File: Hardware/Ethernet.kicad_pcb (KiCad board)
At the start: 2 copper layers, 34 x 34 mm, 41 parts, among them J3 Conn_01x02_Male, J4 Conn_01x02_Male, J5 Conn_01x02_Male, J6 Conn_01x02_Male, J7 Conn_01x08_Male, J9 QWIIC_Stackable, U1 W5500, Y1 25MHz_SMD_Crystal_Resonator

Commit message: Working on SPI
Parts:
- moved R2 4.16 mm to (93.2, 93.0), turned to 180 degrees
- moved RN1 2.04 mm to (91.7, 86.0)
- moved RN2 2.01 mm to (91.7, 89.7)
- moved R6 1.08 mm to (93.0, 100.4)
- moved R8 1.08 mm to (93.0, 98.9)
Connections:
- J7 pad 1: RESET -> WIZ_RST
- J7 pad 2: ATTACH -> SCLK
- J7 pad 4: POWER_OK2 -> MISO
- J7 pad 6: POWER_OK3 -> MOSI
- J7 pad 7: ALERT -> unconnected-(J7-Pad7)
- J7 pad 8: GPIO -> ~{SCS}
- U1 pad 37: IO25_RST -> WIZ_RST
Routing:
- net ~{SCS}: track 0.00 -> 17.4 mm
- net MOSI: track 0.00 -> 14.7 mm, vias 0 -> 1
- net MISO: track 0.00 -> 13.6 mm, vias 0 -> 1
- net WIZ_RST: track 0.00 -> 13.2 mm
- net SCLK: track 0.00 -> 13.0 mm
- net Vsec: track 110.5 -> 116.5 mm
- net Net-(RN1-Pad5): track 3.02 -> 5.45 mm
- net Net-(RN1-Pad6): track 2.89 -> 5.18 mm
- net Net-(RN1-Pad7): track 2.77 -> 4.72 mm
- net Net-(RN1-Pad8): track 2.65 -> 4.29 mm
- net +3.3VA: track 32.4 -> 33.9 mm
- net Net-(RN2-Pad1): track 2.61 -> 3.93 mm
- net Net-(RN2-Pad2): track 2.74 -> 3.80 mm
- net Net-(R2-Pad1): track 2.53 -> 3.43 mm
- net Net-(RN2-Pad3): track 2.86 -> 3.68 mm
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
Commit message: ...
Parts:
- moved R6 7.44 mm to (100.2, 102.3), turned to -90 degrees
- moved R8 6.57 mm to (98.7, 102.2), turned to -90 degrees
- moved R9 3.48 mm to (99.5, 109.7)
- moved R10 2.83 mm to (101.2, 109.7)
- moved C12 2.12 mm to (94.9, 101.5)
- moved R11 2.12 mm to (94.9, 103.0)
- moved R7 1.27 mm to (104.0, 101.9), turned to 180 degrees
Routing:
- net Vsec: track 116.5 -> 107.8 mm
- net TD+: track 18.8 -> 23.7 mm
- net Net-(R9-Pad1): track 2.73 -> 6.21 mm
- net C-YEL: track 26.1 -> 23.2 mm
- net Net-(R10-Pad1): track 2.73 -> 5.57 mm
- net RCT: track 7.85 -> 9.51 mm
- net SCLK: track 13.0 -> 14.6 mm, vias 0 -> 1
- net MISO: track 13.6 -> 15.0 mm, vias 1 -> 0
- net MOSI: track 14.7 -> 16.1 mm, vias 1 -> 0
- net TD-: track 20.2 -> 21.4 mm
- net C-GRN: track 22.2 -> 23.3 mm
- net TCT: track 3.42 -> 4.02 mm
- net RD-: track 23.1 -> 22.5 mm
- net WIZ_RST: track 13.2 -> 13.8 mm

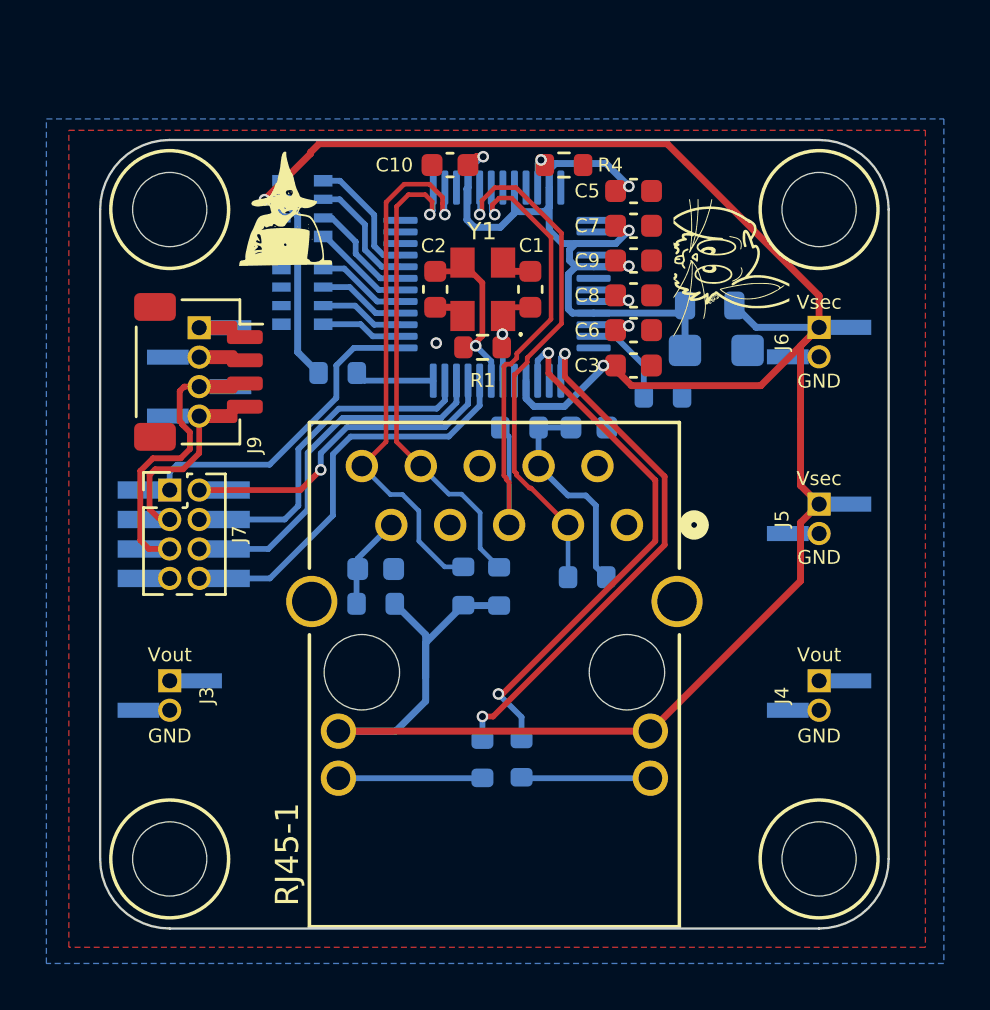
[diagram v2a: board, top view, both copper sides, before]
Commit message: Refining the Ethernet board
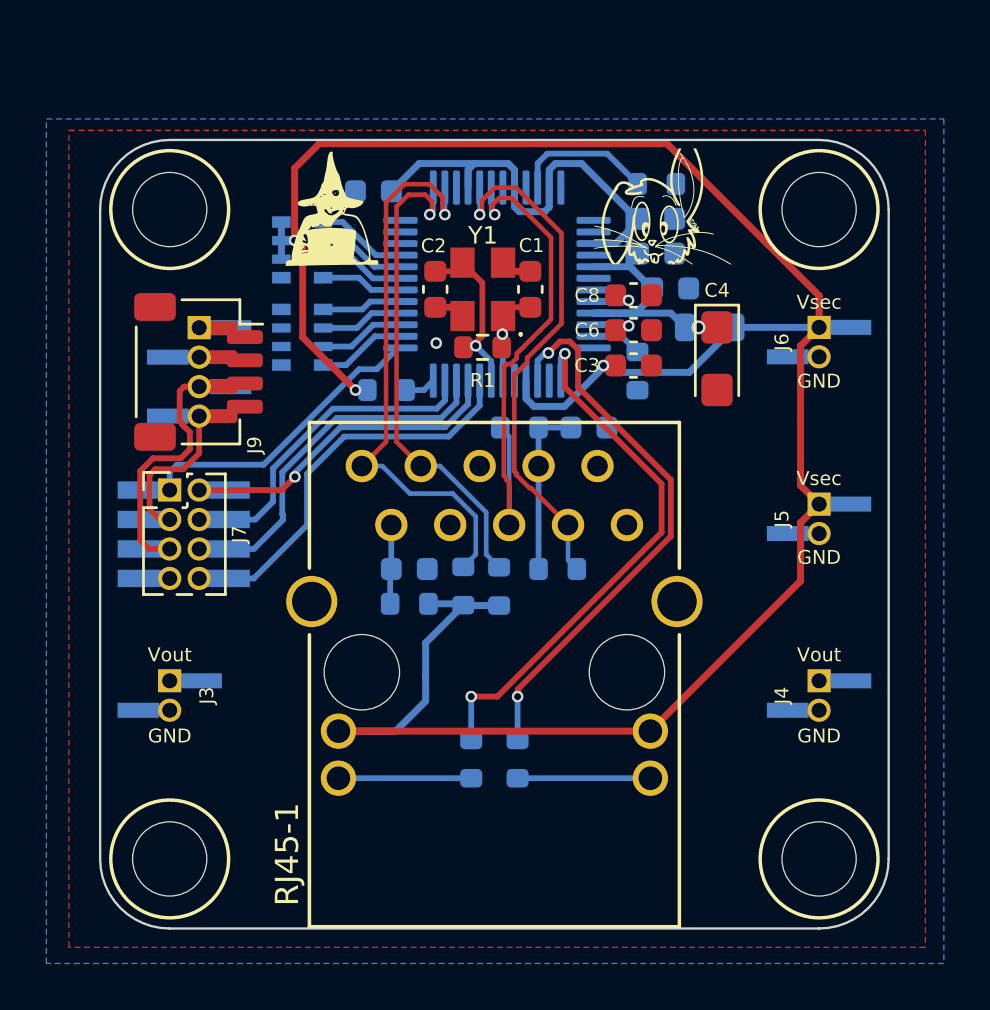
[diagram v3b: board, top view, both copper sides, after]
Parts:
- C10, C5, C7, C9, R4: moved to B.Cu
- C4: value 10uF 6.3V A TANT -> 10uF; moved to F.Cu
- Y1: value 25MHz_SMD_Crystal_Resonator -> 25.000MHz
- moved R4 4.08 mm to (107.0, 84.9)
- moved C10 3.49 mm to (94.8, 85.2)
- moved REF** 3.12 mm to (107.0, 86.5), turned to 0 degrees
- moved R2 2.23 mm to (95.3, 93.8)
- moved G*** 2.00 mm to (93.0, 85.9)
- moved C9 2.00 mm to (107.6, 89.4)
- moved RN1 1.78 mm to (91.7, 87.7)
- moved RN2 1.76 mm to (91.7, 91.5)
- moved C5 1.56 mm to (107.0, 86.4)
- moved C7 1.56 mm to (107.0, 87.9)
- moved R3 1.56 mm to (106.2, 93.0), turned to 90 degrees
- moved C12 1.45 mm to (96.3, 101.5)
- moved R9 1.45 mm to (96.3, 103.0)
- moved R7 1.32 mm to (102.7, 101.5), turned to 0 degrees
- moved L1 0.94 mm to (109.3, 91.1)
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- renumbered R9 to R11, R11 to R9
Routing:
- net Vsec: track 107.8 -> 101.4 mm, vias 2 -> 3
- net Net-(R4-Pad2): track 1.25 -> 6.07 mm, vias 1 -> 0
- net +3.3VA: track 33.9 -> 30.5 mm, vias 4 -> 1
- net Net-(R2-Pad1): track 3.43 -> 1.36 mm
- net RCT: track 9.51 -> 7.50 mm
- net Net-(R3-Pad2): track 4.04 -> 2.17 mm
- net Net-(RN1-Pad5): track 5.45 -> 3.93 mm
- net Net-(RN1-Pad6): track 5.18 -> 3.80 mm
- net TD+: track 23.7 -> 25.0 mm
- net Net-(RN1-Pad7): track 4.72 -> 3.68 mm
- net C-GRN: track 23.3 -> 24.3 mm
- net WIZ_RST: track 13.8 -> 12.9 mm
- net Net-(RN1-Pad8): track 4.29 -> 3.55 mm
- net TCT: track 4.02 -> 3.35 mm
- net MISO: track 15.0 -> 14.4 mm
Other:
- board text added: "Stacked Rabbits ${TITLE} (v${REVISION})"
- board text removed: "NerdMage Modules ${TITLE} (v${REVISION})"

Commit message: Buncha cosmetic stuff...
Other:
- board text added: "Stacked Rabbit ${TITLE} (v${REVISION})"
- board text removed: "Stacked Rabbits ${TITLE} (v${REVISION})"
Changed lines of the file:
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@@
   (gr_line (start 86 117) (end 114 117) (layer "Edge.Cuts") (width 0.1))
   (gr_arc (start 117 114) (mid 116.12132 116.12132) (end 114 117) (layer "Edge.Cuts") (width 0.1))
-  (gr_text "Stacked Rabbits\n${TITLE} (v${REVISION})" (at 100 113) (layer "B.SilkS")
+  (gr_text "Stacked Rabbit\n${TITLE} (v${REVISION})" (at 100 113) (layer "B.SilkS")
     (effects (font (size 1 1) (thickness 0.15)) (justify mirror))
   )

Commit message: More on POE...
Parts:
- added J10: Conn_01x02_Male, Connector_PinSocket_1.27mm:PinSocket_1x02_P1.27mm_Vertical_SMD_Pin1Right, B.Cu at (91.3, 114.0)
- added J11: Conn_01x02_Male, Connector_PinSocket_1.27mm:PinSocket_1x02_P1.27mm_Vertical_SMD_Pin1Right, B.Cu at (108.7, 114.0)
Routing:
- net VB2: track 0.00 -> 25.4 mm, vias 0 -> 1
- net VB1: track 0.00 -> 23.1 mm, vias 0 -> 1
- net VA2: track 0.00 -> 23.0 mm
- net VA1: track 0.00 -> 19.5 mm, vias 0 -> 1
- net Net-(R10-Pad1): vias 0 -> 1
- net Net-(R11-Pad1): vias 0 -> 1

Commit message: Some randomness...
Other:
- board text added: "${TITLE} Board"
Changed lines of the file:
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@@
     (effects (font (size 0.6 0.6) (thickness 0.125)))
+  )
+  (gr_text "${TITLE} Board" (at 110.371547 102.210598 90) (layer "F.SilkS")
+    (effects (font (size 1 1) (thickness 0.15)))
   )
   (gr_text "GND" (at 114 101) (layer "F.SilkS")

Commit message: whole bunche cleanup...
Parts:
- moved REF** 2.06 mm to (109.0, 87.0)
- moved G*** 2.00 mm to (91.0, 86.0)
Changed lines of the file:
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@@
   )
   (footprint "Tinker:DagNabbit" (layer "F.Cu")
-    (at 107 86.5)
+    (at 109 87)
     (attr smd board_only)
     (fp_text reference "REF**" (at 0 -8.08 unlocked) (layer "F.SilkS") hide
@@
   )
   (footprint "Tinker:NerdMage" (layer "F.Cu")
-    (at 93 85.9)
+    (at 91 86)
     (attr board_only exclude_from_pos_files exclude_from_bom)
     (fp_text reference "G***" (at 0 3.81) (layer "F.SilkS") hide
@@
   )
   (footprint "Capacitor_SMD:C_0603_1608Metric" (layer "B.Cu")
-    (at 107 87.9 180)
+    (at 107.017121 87.933233 180)
     (descr "Capacitor SMD 0603 (1608 Metric), square (rectangular) end terminal, IPC_7351 nominal, (Body size source: IPC-SM-782 page 76, https://www.pcb-3d.com/wordpress/wp-content/uploads/ipc-sm-782a_amendment_1_and_2.pdf), generated with kicad-footprint-generator")
     (tags "capacitor")
@@
     (effects (font (size 0.6 0.6) (thickness 0.125)))
   )
-  (gr_text "${TITLE} Board" (at 110.371547 102.210598 90) (layer "F.SilkS")
+  (gr_text "${TITLE} Board" (at 110 100 90) (layer "F.SilkS")
     (effects (font (size 1 1) (thickness 0.15)))
   )
@@
   (segment (start 98.276162 110.520001) (end 99 110.52) (width 0.25) (layer "B.Cu") (net 51))
   (zone (net 21) (net_name "GND") (layer "F.Cu") (hatch edge 0.508)
-    (connect_pads (clearance 0.254))
-    (min_thickness 0.254) (filled_areas_thickness no)
+    (connect_pads (clearance 0.2))
+    (min_thickness 0.2) (filled_areas_thickness no)
     (fill yes (thermal_gap 0.254) (thermal_bridge_width 0.508))
     (polygon

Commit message: Still migrating to 0.2.x
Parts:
- moved J6 1.28 mm to (114.0, 92.4)
- moved J5 0.66 mm to (114.0, 99.4)
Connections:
- net WIZ_RST renamed ~{RESET}
- J7 pad 2: SCLK -> RESET
- J7 pad 3: SCL -> ~{SCS}2
- J7 pad 4: MISO -> SCLK
- J7 pad 5: SDA -> ~{SCS}1
- J7 pad 6: MOSI -> MISO
- J7 pad 7: unconnected-(J7-Pad7) -> ~{SCS}0
- J7 pad 8: ~{SCS} -> MOSI
- U1 pad 32: ~{SCS} -> ~{SCS}0
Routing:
- net ~{SCS}0: track 0.00 -> 20.3 mm
- net ~{SCS}: track 17.6 -> 0.00 mm
- net SDA: track 10.6 -> 0.00 mm
- net SCL: track 6.15 -> 0.00 mm
- net SCLK: track 14.2 -> 16.5 mm
- net Vsec: track 101.4 -> 103.5 mm
- net MISO: track 14.4 -> 16.4 mm
- net MOSI: track 15.9 -> 17.5 mm
- net VB1: track 23.1 -> 22.4 mm
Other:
- board text added: "100 , 80"
- board text added: "2,1,0"
- board text added: "3v3"
- board text added: ">RST"
- board text added: ">~{RST}"
- board text added: "MISO"
- board text added: "MOSI"
- board text added: "SCL"
- board text added: "SCLK"
- board text added: "SDA"
- board text added: "SPI"
- board text added: "Vusb"
- board text added: "~{SCS}"
